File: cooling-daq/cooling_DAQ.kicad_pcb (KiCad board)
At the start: 2 copper layers, 30 x 50 mm, 60 parts, among them J1 Conn_02x10_Odd_Even, J2 Conn_01x03_Pin, J3 Conn_01x02_Pin, J4 Conn_01x02_Pin, J7 USB_C_Receptacle_USB2.0_16P, Q1 2N7002, Q2 2N7002, Q3 Si2301CDS, SW1 SW_SPST, U1 STM32F103C8Tx, U2 AP2204K-ADJ, U3 AP2204K-ADJ, U4 SN65HVD256D, Y1 8M, Y2 32.768k

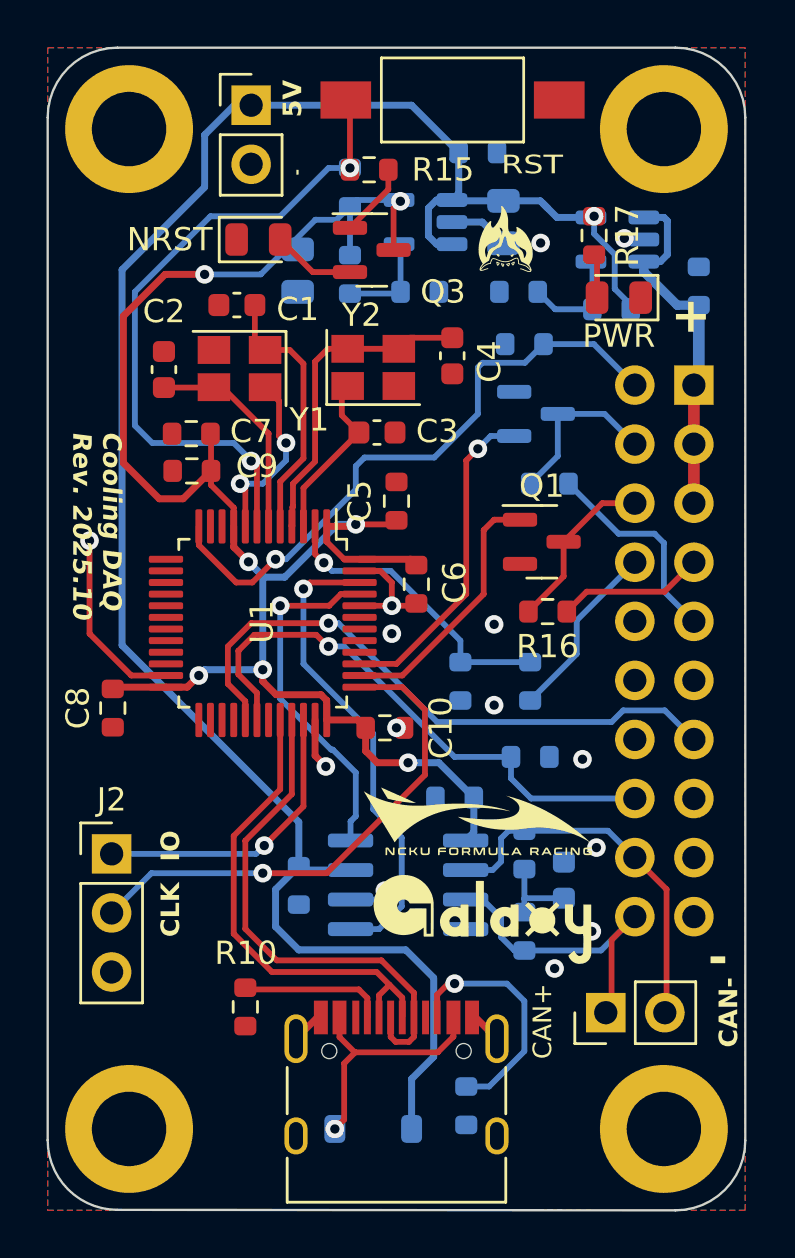
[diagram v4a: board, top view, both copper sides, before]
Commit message: fix: SWDIO LED & CAN jumper
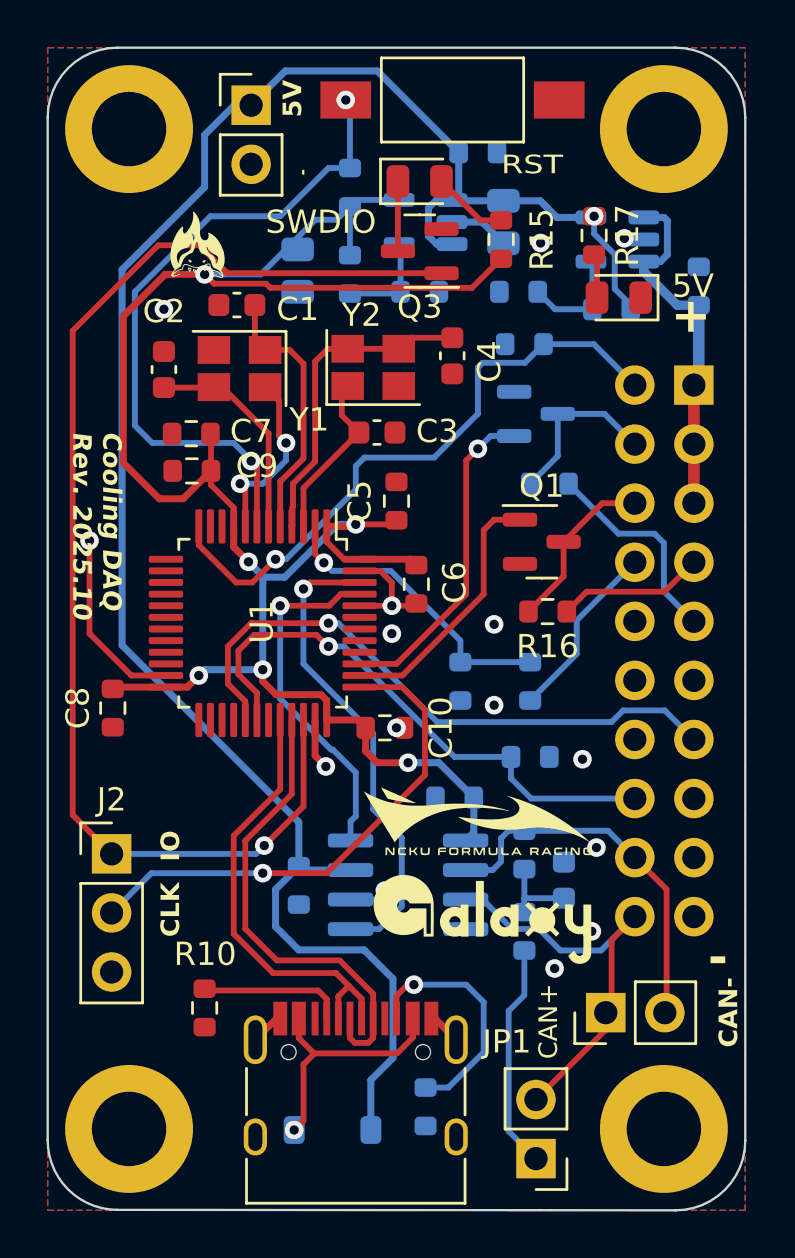
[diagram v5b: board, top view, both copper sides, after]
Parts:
- removed NRST: ~, LED_SMD:LED_0805_2012Metric
- added JP1: Jumper_2_Open, Connector_PinHeader_2.54mm:PinHeader_1x02_P2.54mm_Vertical, F.Cu at (153.0, 141.8)
- added SWDIO: LED, LED_SMD:LED_0805_2012Metric, F.Cu at (148.0, 99.8)
- Q3: value Si2301CDS -> 2N7002
- R15: value 4.7k -> 10k
- moved G*** 13.3 mm to (138.5, 102.5)
- moved R15 6.42 mm to (151.5, 102.2), turned to 90 degrees
- moved Q3 2.06 mm to (148.0, 102.8), turned to 180 degrees
- moved D2 1.75 mm to (144.2, 140.5)
- moved J7 1.75 mm to (145.2, 139.8)
- moved R10 1.75 mm to (138.8, 135.3)
- moved R11 1.75 mm to (148.2, 139.5)
- renumbered PWR to 5V
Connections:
- Q3 pad 1: Net-(Q3-G) -> SYS_JTMS-SWDIO
- Q3 pad 2: Net-(D1-A) -> GND
- Q3 pad 3: +3V3 -> Net-(D1-K)
- R12 pad 1: CAN+ -> Net-(JP1-A)
- R15 pad 1: NRST -> +3V3
- R15 pad 2: Net-(Q3-G) -> Net-(D1-A)
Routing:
- net SYS_JTMS-SWDIO: track 12.8 -> 53.9 mm
- net +3V3: track 75.9 -> 87.2 mm, vias 7 -> 6
- net Net-(JP1-A): track 0.00 -> 9.27 mm
- net CAN+: track 13.3 -> 17.8 mm
- net Net-(Q3-G): track 3.18 -> 0.00 mm
- net Net-(D1-K): track 0.00 -> 3.00 mm
- net USB_D+: track 22.1 -> 20.3 mm
- net USB_D-: track 20.8 -> 19.1 mm
- net +5V: track 86.8 -> 86.3 mm
- net GND: vias 16 -> 17

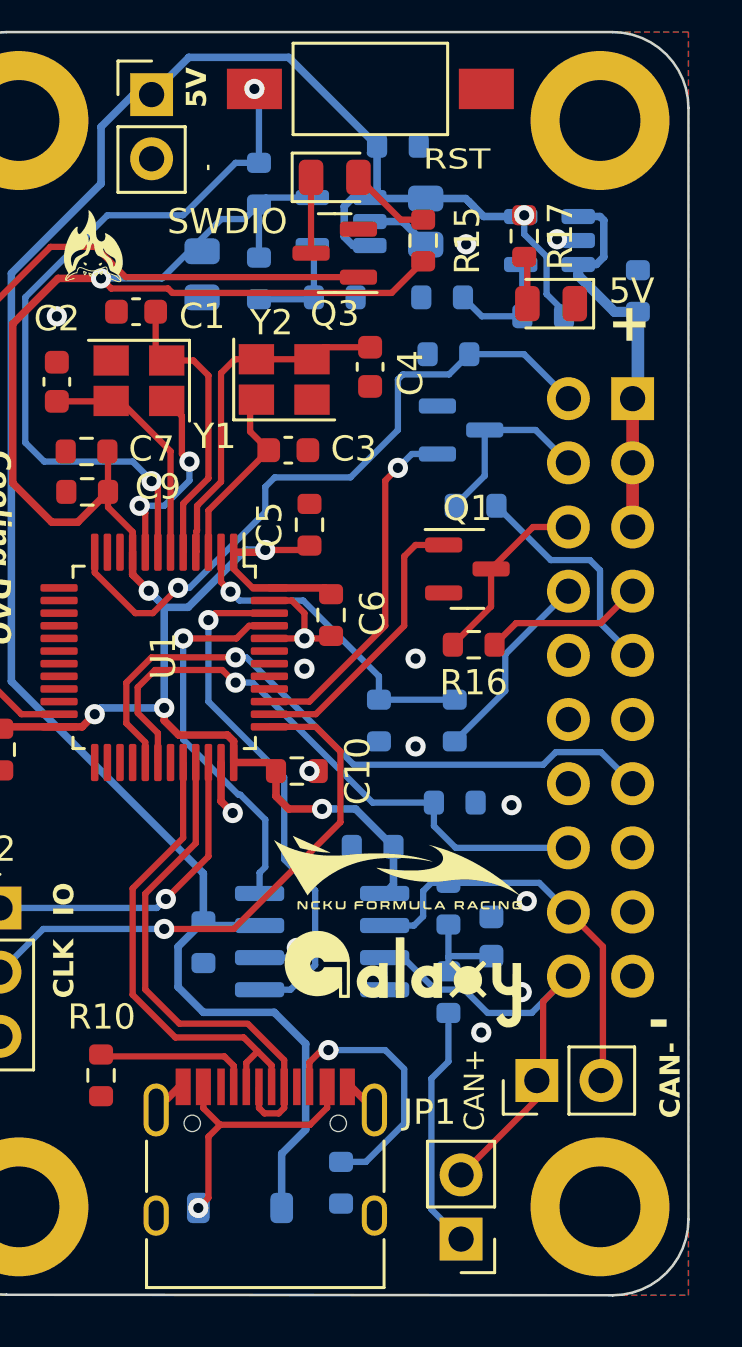
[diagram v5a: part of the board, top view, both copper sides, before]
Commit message: feat: add ESD in CAN
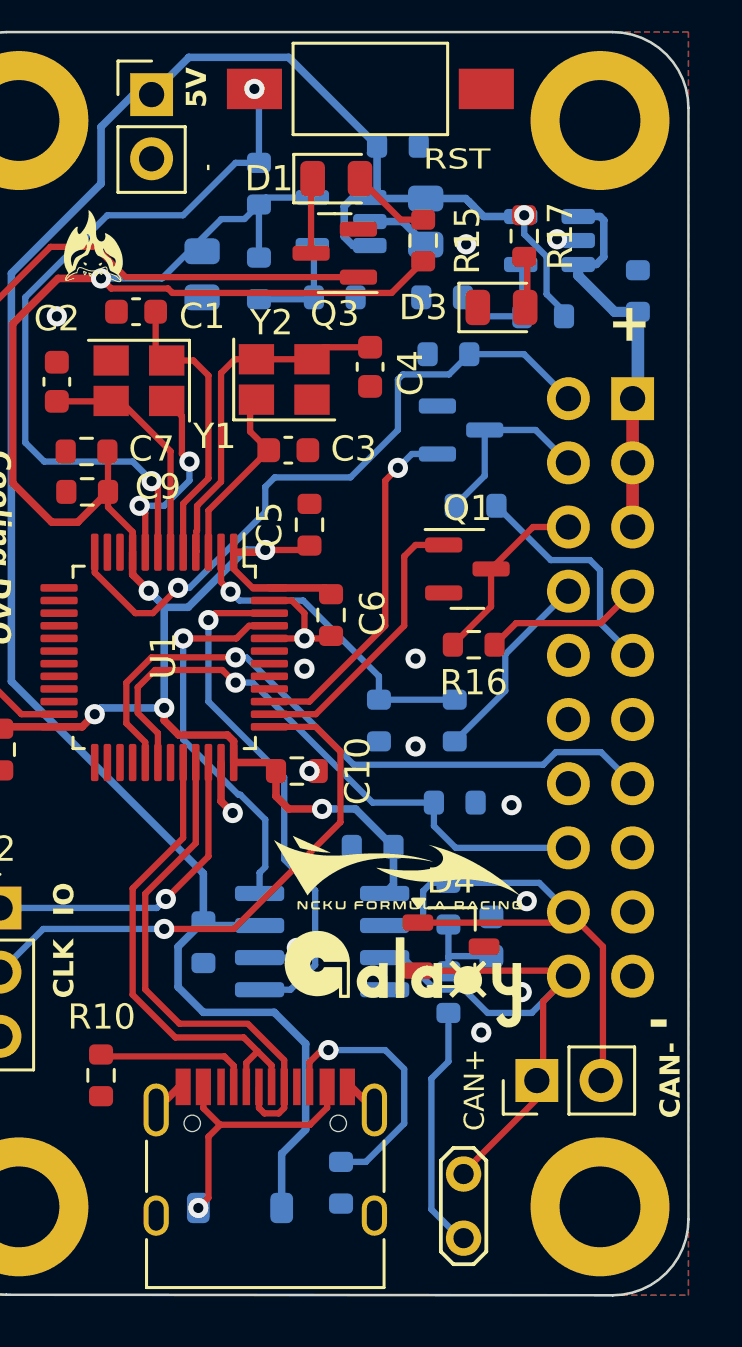
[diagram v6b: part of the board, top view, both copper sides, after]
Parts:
- removed 5V: PWR, LED_SMD:LED_0805_2012Metric
- removed SWDIO: LED, LED_SMD:LED_0805_2012Metric
- added D1: LED, LED_SMD:LED_0805_2012Metric, F.Cu at (148.1, 99.8)
- added D3: PWR, LED_SMD:LED_0805_2012Metric, F.Cu at (154.6, 104.9)
- added D4: DESD2CAN2SOQ, Package_TO_SOT_SMD:TSOT-23, F.Cu at (152.6, 130.2)
- JP1: footprint Connector_PinHeader_2.54mm:PinHeader_1x02_P2.54mm_Vertical -> TestPoint:TestPoint_2Pads_Pitch2.54mm_Drill0.8mm
- moved JP1 2.58 mm to (153.1, 139.2), turned to -90 degrees
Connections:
- JP1 pad 1: Net-(JP1-A) -> CAN+
- JP1 pad 2: CAN+ -> Net-(JP1-B)
- R12 pad 1: Net-(JP1-A) -> Net-(JP1-B)
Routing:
- net Net-(JP1-B): track 0.00 -> 9.27 mm
- net Net-(JP1-A): track 9.27 -> 0.00 mm
- net CAN-: track 16.5 -> 22.7 mm
- net CAN+: track 17.8 -> 23.9 mm

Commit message: feat: redesign
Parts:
- removed C11, C7: 1u, Resistor_SMD:R_0603_1608Metric
- removed C13: 10u, Resistor_SMD:R_0805_2012Metric
- removed C17: 100n, Resistor_SMD:R_0603_1608Metric
- removed C3, C4: 20p, Capacitor_SMD:C_0603_1608Metric
- removed D1: LED, LED_SMD:LED_0805_2012Metric
- removed D2: BAT46W-7-F, Diode_SMD:D_SOD-123
- removed the G*** at (138.5, 102.5)
- removed the G*** at (139.6, 117.3)
- removed J3: Conn_01x02_Pin, Connector_PinHeader_2.54mm:PinHeader_1x02_P2.54mm_Vertical
- removed J7: USB_C_Receptacle_USB2.0_16P, Connector_USB:USB_C_Receptacle_HRO_TYPE-C-31-M-12
- removed Q3: 2N7002, Package_TO_SOT_SMD:SOT-23
- removed R10, R11: 5k1, Resistor_SMD:R_0603_1608Metric
- removed R15, R16: 10k, Resistor_SMD:R_0603_1608Metric
- removed R2: 47k, Resistor_SMD:R_0603_1608Metric
- removed R3, R6: 100k, Resistor_SMD:R_0603_1608Metric
- removed R4: 4.7k, Resistor_SMD:R_0603_1608Metric
- removed R8: 301k, Resistor_SMD:R_0603_1608Metric
- removed SW1: SW_SPST, Button_Switch_SMD:SW_SPST_FSMSM
- removed Y2: 32.768k, Crystal:Crystal_SMD_SeikoEpson_FA238-4Pin_3.2x2.5mm
- added J5: Conn_01x02, Connector_JST:JST_XH_B2B-XH-A_1x02_P2.50mm_Vertical, F.Cu at (39.0, 138.0)
- added kibuzzard-6A0E14C0: G***, kibuzzard-6A0E14C0, F.Cu at (33.8, 132.6)
- C12, C14, C15, C16, Q2, R12, R13, R14, R5, R7, R9, U3, U4: moved to F.Cu
- J1: value Conn_02x10_Odd_Even -> Conn_PWR; footprint Connector_PinHeader_2.54mm:PinHeader_2x10_P2.54mm_Vertical -> Connector_JST:JST_XH_B2B-XH-A_1x02_P2.50mm_Vertical; moved to F.Cu
- J4: value Conn_01x02_Pin -> Conn_01x04; footprint Connector_PinHeader_2.54mm:PinHeader_1x02_P2.54mm_Vertical -> Connector_JST:JST_XH_B4B-XH-A_1x04_P2.50mm_Vertical
- R1: value 4.7k -> 10k; moved to F.Cu
- U2: value AP2204K-ADJ -> TME-2405S; footprint Package_TO_SOT_SMD:SOT-23-5 -> Converter_DCDC:Converter_DCDC_TRACO_TME_24xxS_Single_THT; moved to F.Cu
- moved H1 129.8 mm to (29.0, 107.0)
- moved U2 129.7 mm to (27.3, 113.3), turned to 0 degrees
- moved J1 123.8 mm to (36.0, 106.0), turned to 0 degrees
- moved R17 121.1 mm to (35.0, 114.2), turned to 0 degrees
- moved U3 120.6 mm to (30.6, 128.2)
- moved C12 120.3 mm to (34.0, 128.4), turned to -90 degrees
- moved D3 119.7 mm to (35.1, 112.2)
- moved R9 119.5 mm to (27.5, 125.5), turned to 0 degrees
- moved R7 119.1 mm to (30.8, 125.5)
- moved C14 118.7 mm to (26.7, 128.2), turned to 90 degrees
- moved JP1 115.6 mm to (37.7, 132.5), turned to 0 degrees
- moved R14 111.9 mm to (41.7, 111.0), turned to 180 degrees
- moved R13 109.6 mm to (43.2, 136.8), turned to -90 degrees
- moved R12 109.3 mm to (43.2, 133.5), turned to -90 degrees
- moved C6 108.1 mm to (39.8, 116.6), turned to 180 degrees
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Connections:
- net NRST renamed Net-(U1-NRST)
- J1 pad 1: VDC -> GND
- J1 pad 2: USART2 -> Net-(J1-Pin_2)
- J4 pad 2: GND -> FAN_PWM
- Q1 pad 1: PWM_OUT -> PWM_OUT_2
- Q1 pad 3: PUMP_PWM -> FAN_PWM2
- Q2 pad 1: PWM_OUT_2 -> PWM_OUT
- R1 pad 1: USART2 -> FAN_PWM2
- R1 pad 2: GND -> +5V
- R14 pad 2: FAN_PWR -> +5V
- U1 pad 2: ADC_CH1 -> unconnected-(U1-PC13-Pad2)
- U1 pad 3: /LSE_IN -> unconnected-(U1-PC14-Pad3)
- U1 pad 4: /LSE_OUT -> unconnected-(U1-PC15-Pad4)
- U2 pad 1: VDC -> GND
- U2 pad 2: GND -> Net-(J1-Pin_2)
- U2 pad 3: VDC -> GND
- U2 pad 4: Net-(U2-ADJ) -> +5V
- U4 pad 8: unconnected-(U4-S-Pad8) -> GND
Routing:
- net SYS_JTMS-SWDIO: track 53.9 -> 7.92 mm, vias 1 -> 0
- net USART2: track 27.0 -> 0.00 mm, vias 1 -> 0
- net TIM1_CH1: track 26.6 -> 0.00 mm, vias 1 -> 0
- net USART1: track 24.1 -> 0.00 mm, vias 1 -> 0
- net GND: track 31.3 -> 7.88 mm, vias 17 -> 6
- net Net-(U1-NRST): track 29.0 -> 7.23 mm, vias 2 -> 0
- net USB_D+: track 20.3 -> 0.00 mm
- net USB_D-: track 19.1 -> 0.00 mm
- net VDC: track 15.7 -> 0.00 mm
- net Net-(J1-Pin_2): track 0.00 -> 15.3 mm
- net /LSE_OUT: track 13.9 -> 0.00 mm
- net +5V: track 86.3 -> 72.7 mm, vias 1 -> 0
- net ADC_CH1: track 12.9 -> 0.00 mm, vias 1 -> 0
- net SYS_JTCK-SWCLK: track 21.9 -> 9.14 mm
- net CAN_TX: track 20.5 -> 8.65 mm, vias 1 -> 0
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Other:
- board size 30 x 50 mm -> 40 x 40 mm
- board text added: "Cooling DAQ Rev. 2026.05"
- board text removed: "-"
- board text removed: "5V"
- board text removed: "CAN+"
- board text removed: "CAN-"
- board text removed: "CLK"
- board text removed: "Cooling DAQ Rev. 2025.10"
- board text removed: "IO"
- board text removed: "RST"
